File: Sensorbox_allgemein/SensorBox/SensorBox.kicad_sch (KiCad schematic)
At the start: 27 parts, among them J1 SD_Card, Q1 NPN, U1 LM2596S-3.3, U2 PS1-O3-100, U3 Beetle ESP32-C6, U5 HPP845E131R5

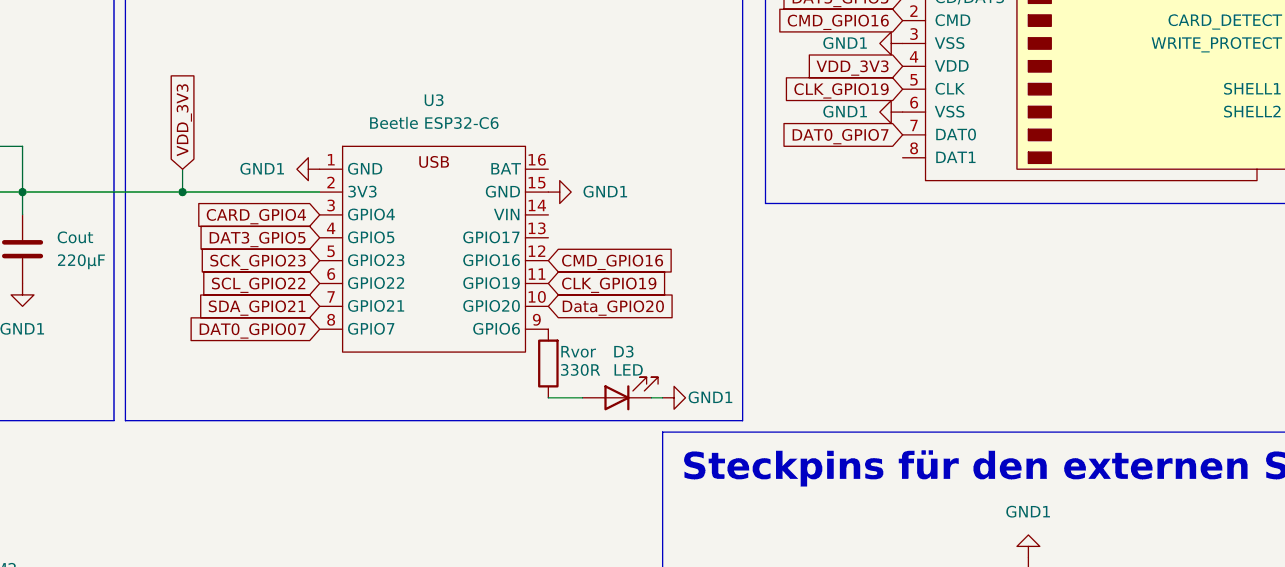
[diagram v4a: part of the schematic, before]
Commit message: Update SensorBox.kicad_sch
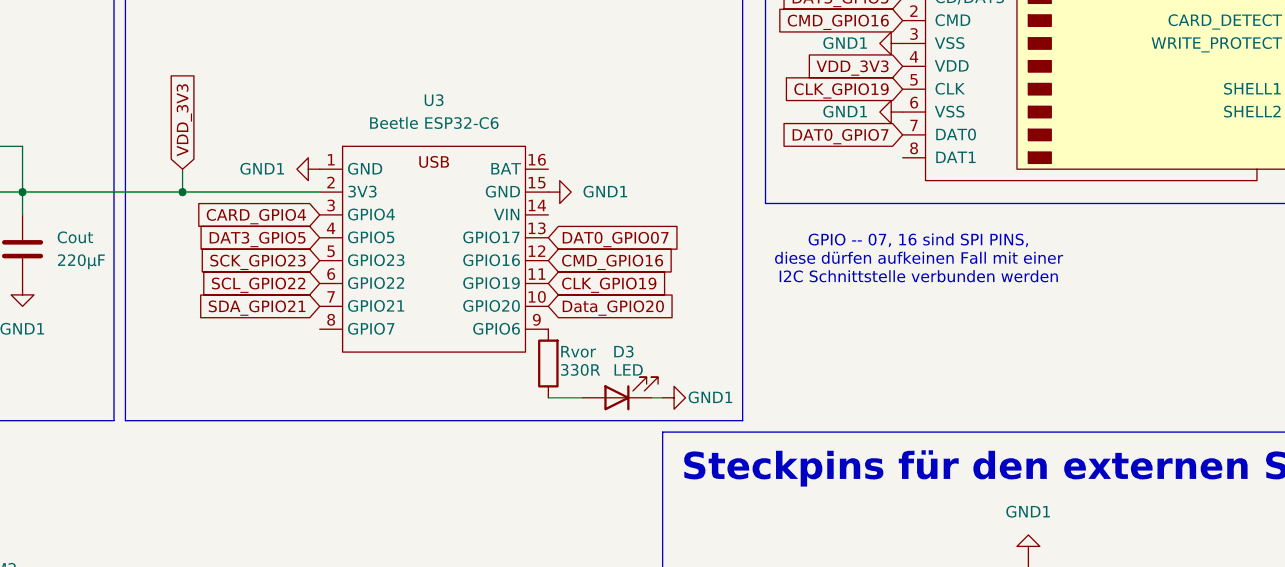
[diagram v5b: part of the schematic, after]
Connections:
- net DAT0_GPIO07: now also U3.13 (GPIO17); no longer U3.8 (GPIO7)
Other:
- note added: "GPIO -- 07, 16 sind SPI PINS, diese dürfen aufkeinen Fall mit einer I2C Schnittstelle verbunden werden"
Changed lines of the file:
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@@
+		)
+	)
+	(text "GPIO -- 07, 16 sind SPI PINS, \ndiese dürfen aufkeinen Fall mit einer \nI2C Schnittstelle verbunden werden"
+		(exclude_from_sim no)
+		(at 222.758 62.23 0)
+		(effects
+			(font
+				(size 1.27 1.27)
+			)
 		)
 	)
@@
 		)
 	)
+	(global_label "DAT0_GPIO07"
+		(shape input)
+		(at 181.61 59.69 0)
+		(fields_autoplaced yes)
+		(effects
+			(font
+				(size 1.27 1.27)
+			)
+			(justify left)
+		)
+		(property "Intersheetrefs" "${INTERSHEET_REFS}"
+			(at 196.9928 59.69 0)
+			(effects
+				(font
+					(size 1.27 1.27)
+				)
+				(justify left)
+				(hide yes)
+			)
+		)
+	)
 	(global_label "Steuerung_VCC"
 		(shape input)
@@
 			(effects
 				(font
-					(size 1.27 1.27)
-				)
-				(justify right)
-				(hide yes)
-			)
-		)
-	)
-	(global_label "DAT0_GPIO07"
-		(shape input)
-		(at 156.21 69.85 180)
-		(fields_autoplaced yes)
-		(effects
-			(font
-				(size 1.27 1.27)
-			)
-			(justify right)
-		)
-		(property "Intersheetrefs" "${INTERSHEET_REFS}"
-			(at 140.8272 69.85 0)
-			(effects
-				(font

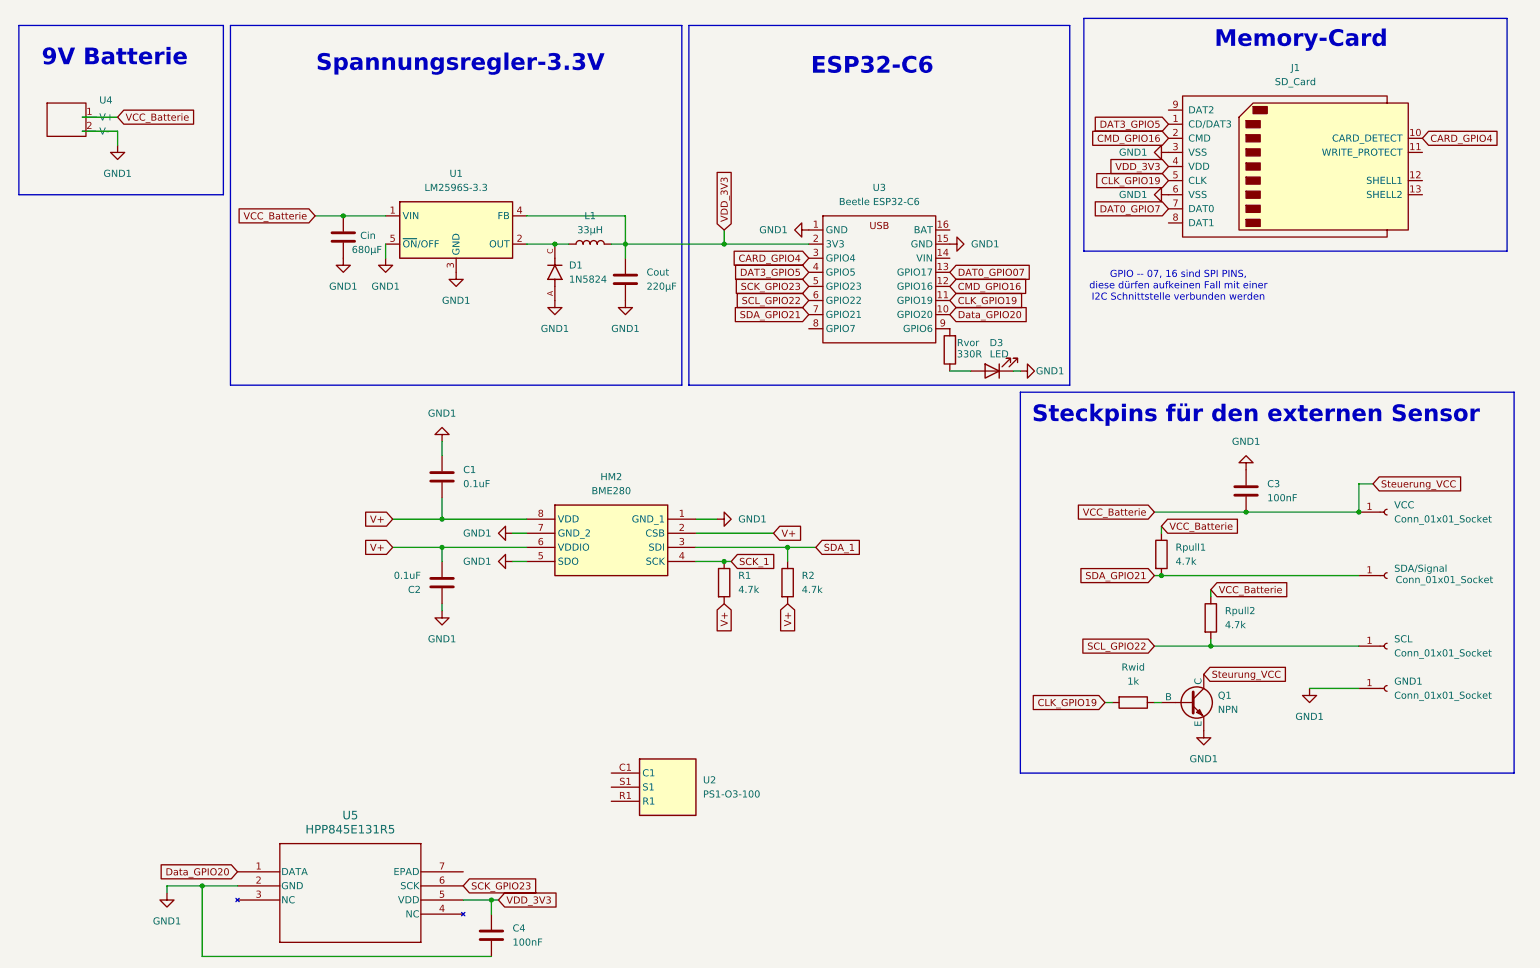
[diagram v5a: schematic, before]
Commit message: Update SensorBox.kicad_sch
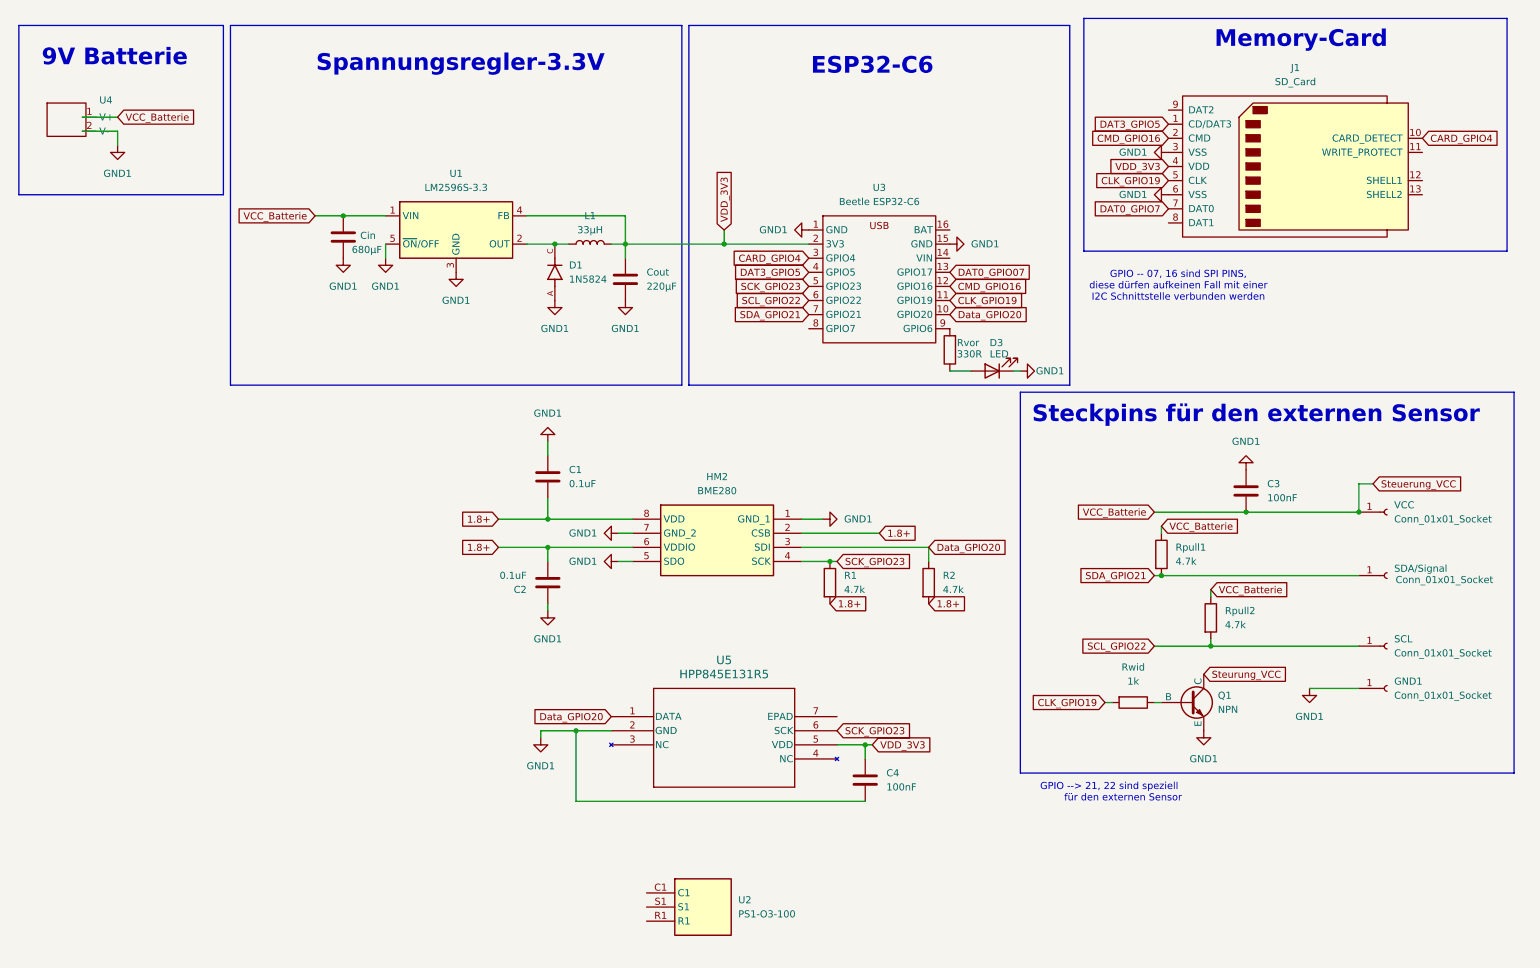
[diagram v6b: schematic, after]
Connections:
- net SCK_1 is gone; now on net SCK_GPIO23: HM2.4 (SCK), R1.1
- net SDA_1 is gone; now on net Data_GPIO20: HM2.3 (SDI), R2.1
- net V+ renamed 1.8+
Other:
- note added: "GPIO --> 21, 22 sind speziell für den externen Sensor"
- moved on the sheet: C1, C2, C4, HM2, R1, R2, U2, U5

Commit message: schaltplan änderungen
spannungswandler und pins geändert
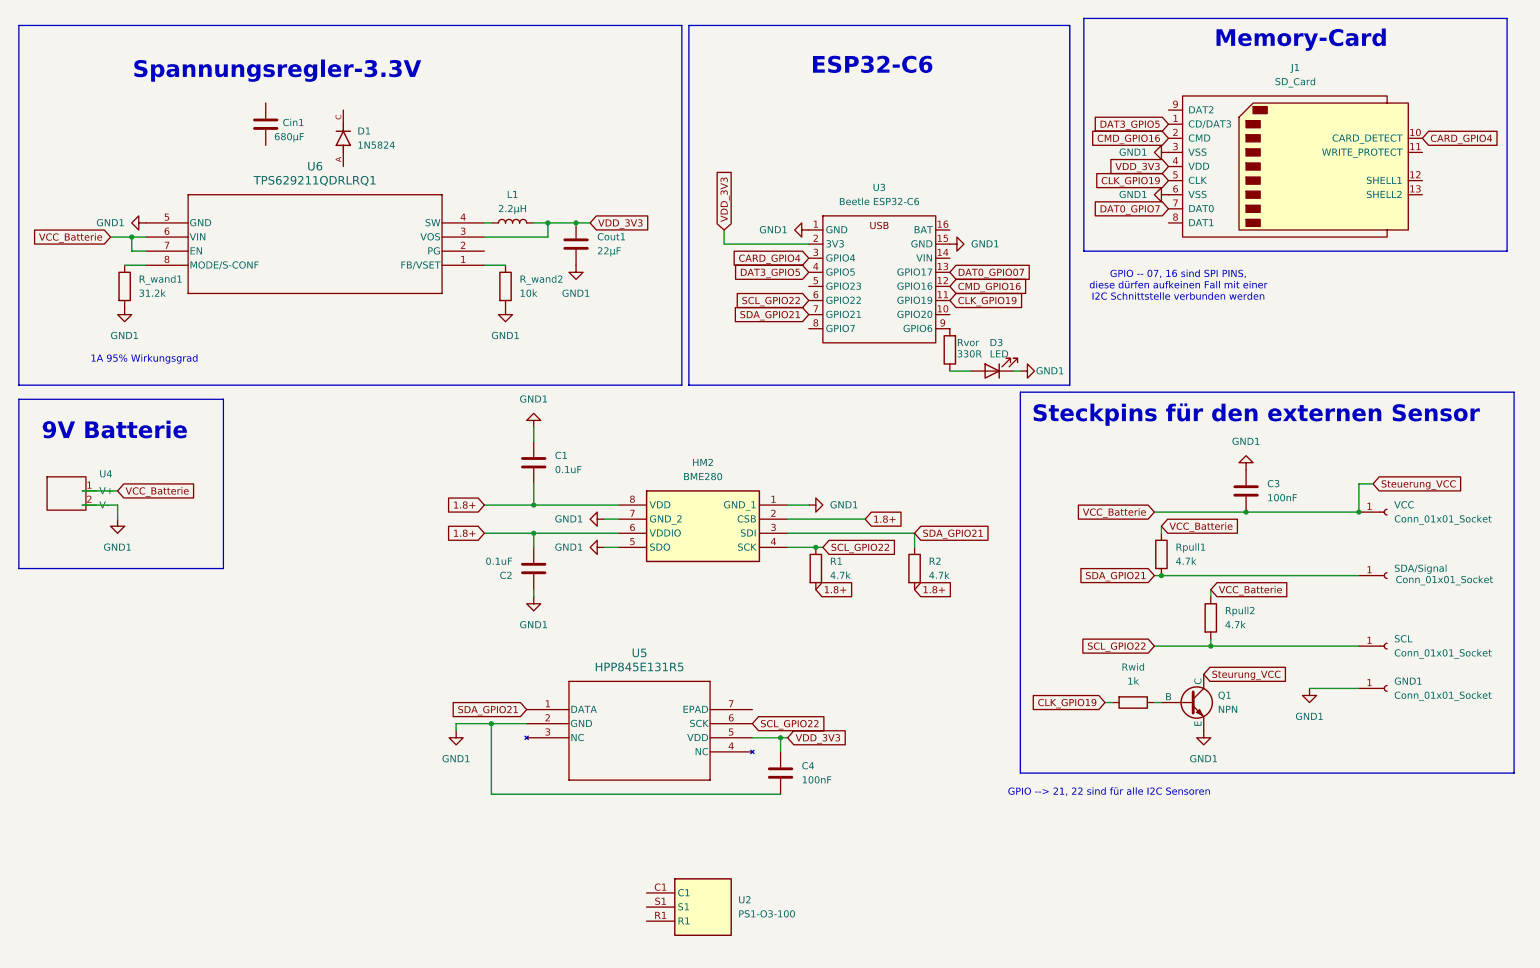
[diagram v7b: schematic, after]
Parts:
- removed Cin: 680µF, Capacitor_SMD:C_0402_1005Metric_Pad0.74x0.62mm_HandSolder, symbol Device:C
- removed Cout: 220µF, Capacitor_SMD:C_0402_1005Metric_Pad0.74x0.62mm_HandSolder, symbol Device:C
- removed U1: LM2596S-3.3, Package_TO_SOT_SMD:TO-263-5_TabPin3, symbol Regulator_Switching:LM2596S-3.3
- added Cin1: 680µF, Capacitor_SMD:C_0402_1005Metric_Pad0.74x0.62mm_HandSolder, symbol Device:C
- added Cout1: 22µF, Capacitor_SMD:C_0402_1005Metric_Pad0.74x0.62mm_HandSolder, symbol Device:C
- added R_wand1: 31.2k, Resistor_SMD:R_0402_1005Metric, symbol Device:R
- added R_wand2: 10k, Resistor_SMD:R_0402_1005Metric, symbol Device:R
- added U6: TPS629211QDRLRQ1, footprints:SOT5X3_DRL_TEX, symbol 2024-11-18_14-00-38:TPS629211QDRLRQ1
- L1: value 33µH -> 2.2µH
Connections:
- net GND1: now also Cout1.2, R_wand1.2, R_wand2.2, U6.5 (GND); no longer D1.A
- net SCL_GPIO22: now also HM2.4 (SCK), R1.1, U5.6 (SCK)
- net SDA_GPIO21: now also HM2.3 (SDI), R2.1, U5.1 (DATA)
- net Steuerung_VCC: now also U6.6 (VIN), U6.7 (EN)
- net VDD_3V3: now also Cout1.1, U6.3 (VOS)
- net at D1.C: no longer L1.1
- removed net Data_GPIO20: HM2.3 (SDI), R2.1, U3.10 (GPIO20), U5.1 (DATA)
- removed net SCK_GPIO23: HM2.4 (SCK), R1.1, U3.5 (GPIO23), U5.6 (SCK)
- new net: R_wand1.1, U6.8 (MODE/S-CONF)
- new net: L1.1, U6.4 (SW)
- new net: R_wand2.1, U6.1 (FB/VSET)
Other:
- note added: "1A 95% Wirkungsgrad"
- note added: "GPIO --> 21, 22 sind für alle I2C Sensoren"
- note removed: "GPIO --> 21, 22 sind speziell für den externen Sensor"
- moved on the sheet: C1, C2, C4, HM2, R1, R2, U4, U5
